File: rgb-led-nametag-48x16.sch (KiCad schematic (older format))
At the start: 41 parts, among them J1 USB_C_Receptacle_USB2.0, J2 TagConnect_TC2030_SWD, Q17 CJ3139K, Q18 CJ3139K, Q19 2SK3541, Q20 AO3401A, U25 STM32F722RETx, U26 SRV05-4, U27 TPS63001, U28 XC6206P332MR

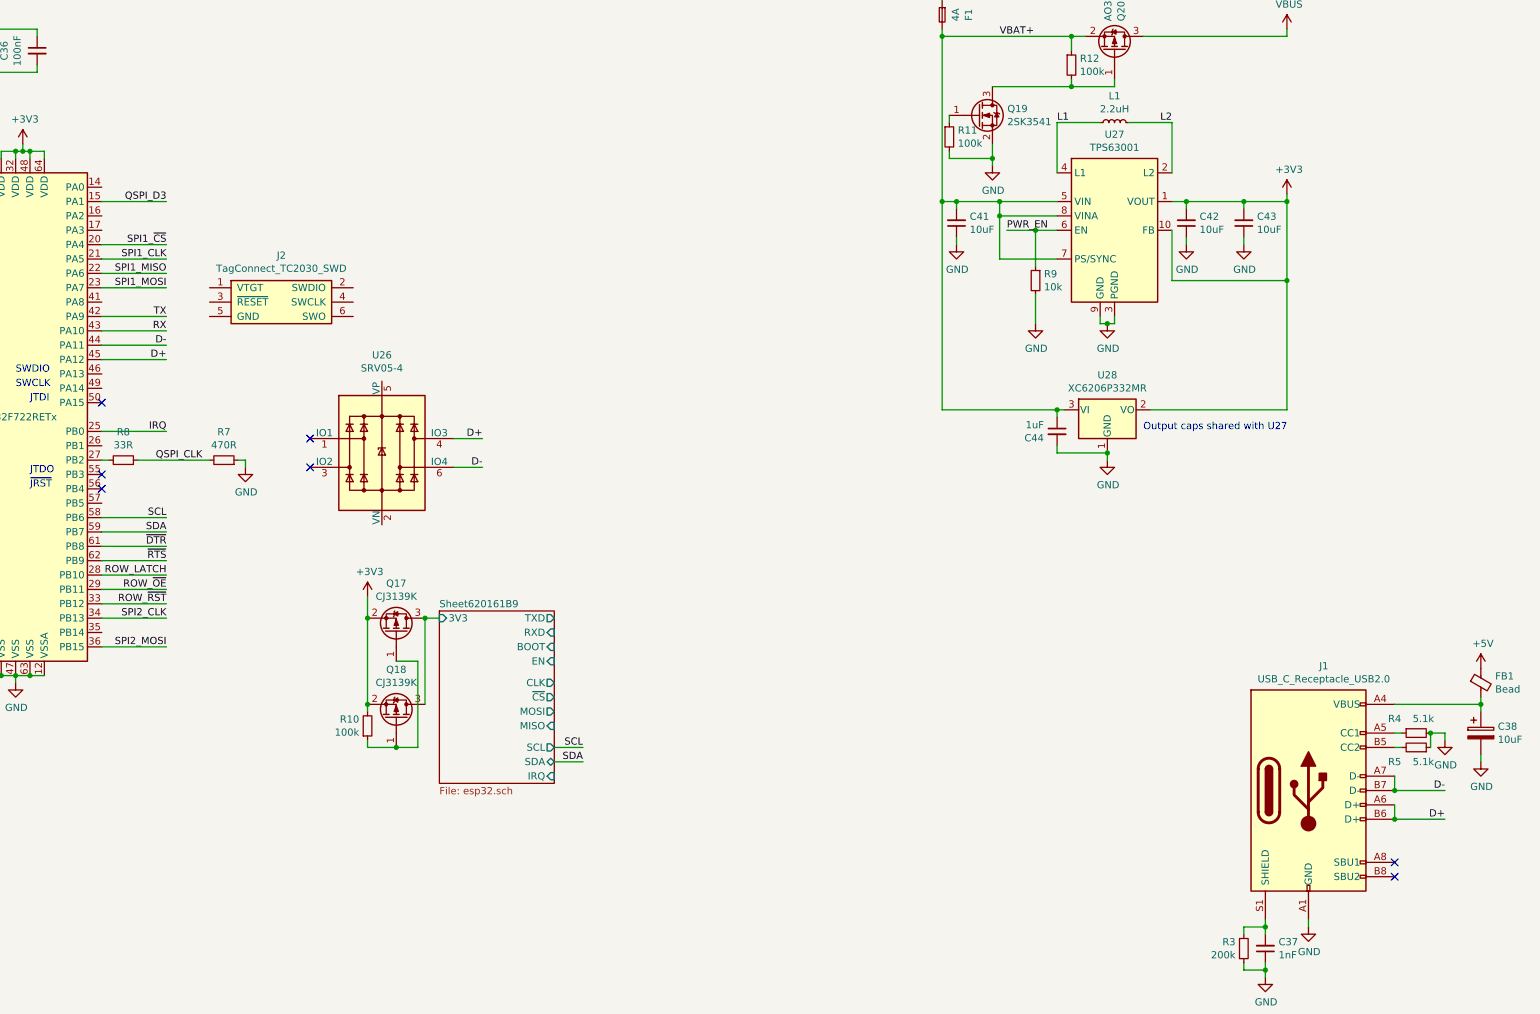
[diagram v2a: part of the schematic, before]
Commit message: Connect SWD to USB type C SBU
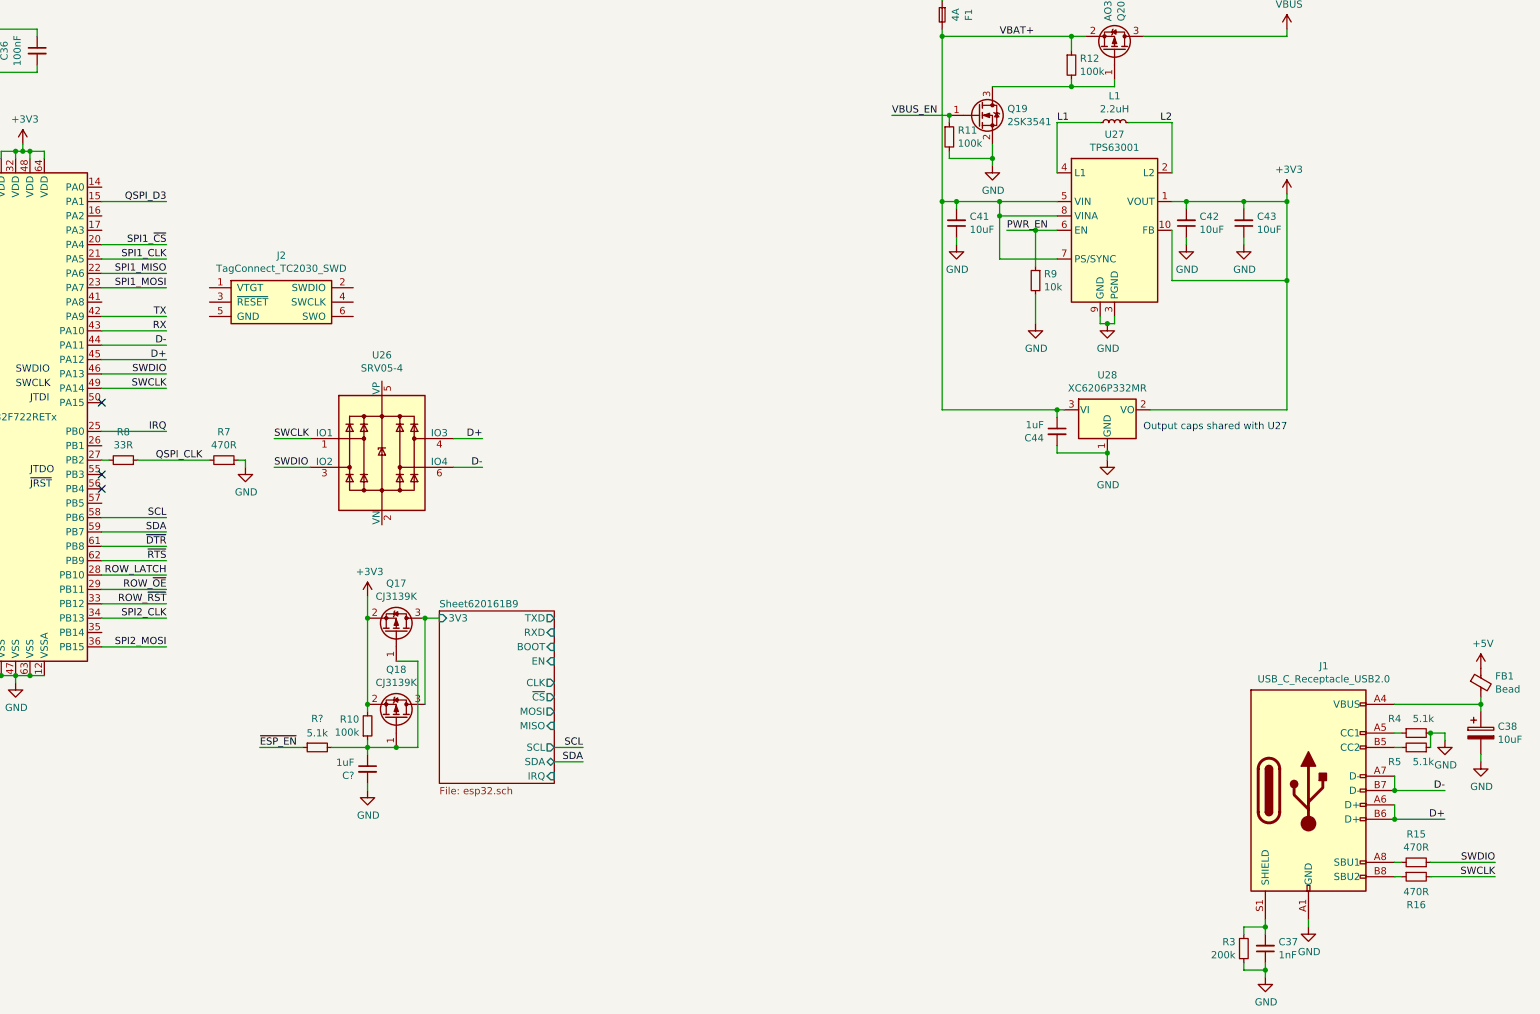
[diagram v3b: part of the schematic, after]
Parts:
- added C?: 1uF, Capacitor_SMD:C_0402_1005Metric, symbol Device:C_Small
- added R15, R16: 470R, Resistor_SMD:R_0402_1005Metric, symbol Device:R_Small
- added R?: 5.1k, Resistor_SMD:R_0402_1005Metric, symbol Device:R_Small
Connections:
- net GND: now also C?.2
- net SWDIO: now reaches U25.46 (PA13)
- net SWDIO: now also U26.3 (IO2), R15.1
- net SWCLK: now reaches U25.49 (PA14)
- net SWCLK: now also U26.1 (IO1), R16.2
- net at J1.A8 (SBU1): now also R15.2
- net at J1.B8 (SBU2): now also R16.1
- net at Q17.1 (G), Q18.1 (G), R10.1: now also C?.1, R?.2
- net VBUS_EN: now reaches Q19.1 (G), R11.1
- new net ~ESP_EN: R?.1
- no-connect marks 11 -> 7
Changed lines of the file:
@@
 D+
 Connection ~ 16400 6450
-NoConn ~ 16400 6750
-NoConn ~ 16400 6850
 $Comp
 L power:GND #PWR0176
@@
 	1    0    0    -1
 $EndComp
-NoConn ~ 8850 3800
-NoConn ~ 8850 4000
 $Comp
 L Device:R_Small R8
@@
 Wire Wire Line
 	10750 6050 10550 6050
-Wire Bus Line
-	2950 1250 2950 6650
 Wire Wire Line
 	14700 3600 15650 3600
 Text Notes 14650 3750 0    50   ~ 0
 Output caps shared with U27
+Wire Wire Line
+	7400 3350 7850 3350
+Text Label 7850 3350 2    50   ~ 0
+SWDIO
+Wire Wire Line
+	7400 3450 7850 3450
+Text Label 7850 3450 2    50   ~ 0
+SWCLK
+Wire Wire Line
+	16650 6750 17100 6750
+Text Label 17100 6750 2    50   ~ 0
+SWDIO
+Wire Wire Line
+	16650 6850 17100 6850
+Text Label 17100 6850 2    50   ~ 0
+SWCLK
+Text Label 8600 3800 0    50   ~ 0
+SWCLK
+Wire Wire Line
+	8600 3800 8850 3800
+$Comp
+L Device:R_Small R15
+U 1 1 62A6EAFE
+P 16550 6750
+F 0 "R15" V 16746 6750 50  0000 C CNN
+F 1 "470R" V 16655 6750 50  0000 C CNN
+F 2 "Resistor_SMD:R_0402_1005Metric" H 16550 6750 50  0001 C CNN
+F 3 "~" H 16550 6750 50  0001 C CNN
+F 4 "C25117" H 16550 6750 50  0001 C CNN "LCSC"
+	1    16550 6750
+	0    1    -1   0
+$EndComp
+$Comp
+L Device:R_Small R16
+U 1 1 62A82547
+P 16550 6850
+F 0 "R16" V 16746 6850 50  0000 C CNN
+F 1 "470R" V 16655 6850 50  0000 C CNN
+F 2 "Resistor_SMD:R_0402_1005Metric" H 16550 6850 50  0001 C CNN
+F 3 "~" H 16550 6850 50  0001 C CNN
+F 4 "C25117" H 16550 6850 50  0001 C CNN "LCSC"
+	1    16550 6850
+	0    -1   1    0
+$EndComp
+Wire Wire Line
+	16450 6750 16400 6750
+Wire Wire Line
+	16400 6850 16450 6850
+Wire Wire Line
+	8600 4000 8850 4000
+Text Label 8600 4000 0    50   ~ 0
+SWDIO
+$Comp
+L Device:C_Small C?
+U 1 1 62B47E57
+P 9250 6100
+AR Path="/620161BA/62B47E57" Ref="C?"  Part="1"
+AR Path="/62B47E57" Ref="C?"  Part="1"
+F 0 "C?" H 9158 6054 50  0000 R CNN
+F 1 "1uF" H 9158 6145 50  0000 R CNN
+F 2 "Capacitor_SMD:C_0402_1005Metric" H 9250 6100 50  0001 C CNN
+F 3 "~" H 9250 6100 50  0001 C CNN
+F 4 "C52923" H 9250 6100 50  0001 C CNN "LCSC"
+	1    9250 6100
+	1    0    0    -1
+$EndComp
+$Comp
+L power:GND #PWR?
+U 1 1 62B5C3F7
+P 9250 6250
+F 0 "#PWR?" H 9250 6000 50  0001 C CNN
+F 1 "GND" H 9255 6077 50  0000 C CNN
+F 2 "" H 9250 6250 50  0001 C CNN
+F 3 "" H 9250 6250 50  0001 C CNN
+	1    9250 6250
+	1    0    0    -1
+$EndComp
+Wire Wire Line
+	9250 6250 9250 6200
+Wire Wire Line
+	9250 6000 9250 5950
+Connection ~ 9250 5950
+$Comp
+L Device:R_Small R?
+U 1 1 62B8632F
+P 8900 5950
+F 0 "R?" V 8700 5950 50  0000 C CNN
+F 1 "5.1k" V 8800 5950 50  0000 C CNN
+F 2 "Resistor_SMD:R_0402_1005Metric" H 8900 5950 50  0001 C CNN
+F 3 "~" H 8900 5950 50  0001 C CNN
+F 4 "C23186" H 8900 5950 50  0001 C CNN "LCSC"
+	1    8900 5950
+	0    -1   1    0
+$EndComp
+Wire Wire Line
+	9000 5950 9250 5950
+Text Label 8500 5950 0    50   ~ 0
+~ESP_EN
+Wire Wire Line
+	8500 5950 8800 5950
+Connection ~ 13300 1550
+Text Label 12900 1550 0    50   ~ 0
+VBUS_EN
+Wire Wire Line
+	12900 1550 13300 1550
+Wire Bus Line
+	2950 1250 2950 6650
 $EndSCHEMATC

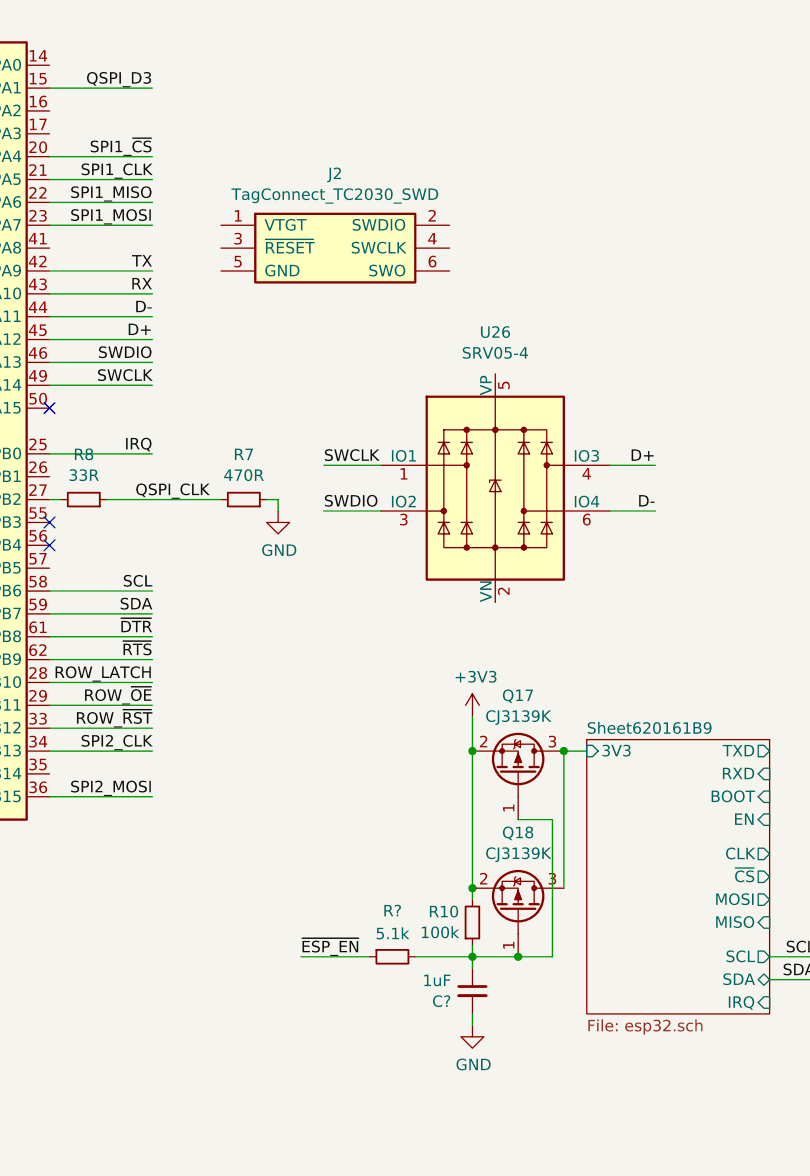
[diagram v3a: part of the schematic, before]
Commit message: Wire column mux SPI
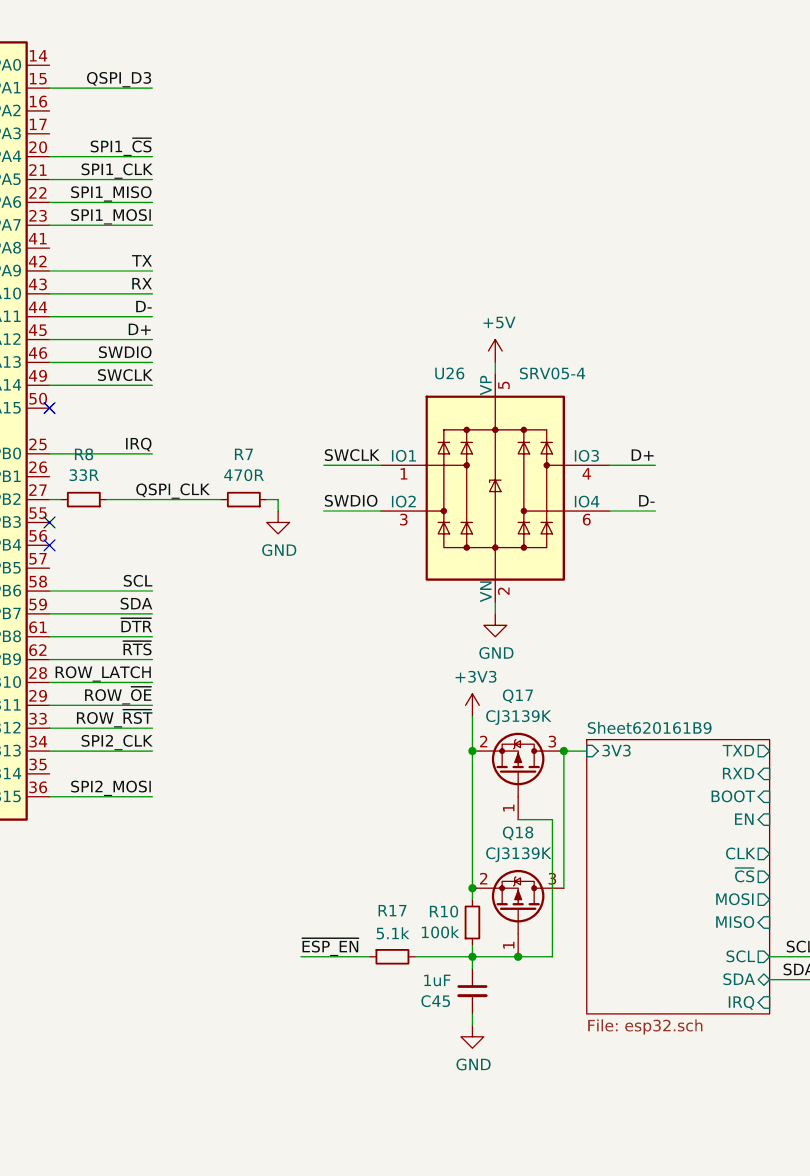
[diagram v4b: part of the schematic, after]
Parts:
- removed J2: TagConnect_TC2030_SWD, Connector:Tag-Connect_TC2030-IDC-NL_2x03_P1.27mm_Vertical, symbol Connector_TagConnect:TagConnect_TC2030_SWD
- gave numbers to parts that had none: 2
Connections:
- net +5V: now also U26.5 (VP)
- net GND: now also U26.2 (VN)
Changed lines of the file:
@@
 Text Label 7850 2750 2    50   ~ 0
 SPI1_MOSI
-Text Label 7850 5050 2    50   ~ 0
-SPI2_CLK
-Text Label 7850 5250 2    50   ~ 0
-SPI2_MOSI
 Text Label 1150 2900 0    50   ~ 0
 SPI2_MOSI
@@
 Wire Wire Line
 	6100 4450 5650 4450
-Text Label 7850 4750 2    50   ~ 0
-ROW_LATCH
-Wire Wire Line
-	7400 4750 7850 4750
 Text Label 7850 4850 2    50   ~ 0
 ROW_~OE
@@
 Wire Wire Line
 	7400 4650 7850 4650
-Wire Wire Line
-	7400 5050 7850 5050
-Wire Wire Line
-	7400 5250 7850 5250
 Wire Wire Line
 	7400 2750 7850 2750
@@
 Connection ~ 15500 7500
 $Comp
-L Connector_TagConnect:TagConnect_TC2030_SWD J2
-U 1 1 620AEB39
-P 8650 2850
-F 0 "J2" H 8650 3175 50  0000 C CNN
-F 1 "TagConnect_TC2030_SWD" H 8650 3084 50  0000 C CNN
-F 2 "Connector:Tag-Connect_TC2030-IDC-NL_2x03_P1.27mm_Vertical" H 8650 2850 50  0001 C CNN
-F 3 "" H 8650 2850 50  0001 C CNN
-	1    8650 2850
-	1    0    0    -1
-$EndComp
-$Comp
 L Regulator_Switching:TPS63001 U27
 U 1 1 620B2056
@@
 U 1 1 61FD5228
 P 9350 3900
-F 0 "U26" H 9350 4581 50  0000 C CNN
-F 1 "SRV05-4" H 9350 4490 50  0000 C CNN
+F 0 "U26" H 9150 4400 50  0000 C CNN
+F 1 "SRV05-4" H 9600 4400 50  0000 C CNN
 F 2 "Package_TO_SOT_SMD:SOT-23-6" H 10050 3450 50  0001 C CNN
 F 3 "http://www.onsemi.com/pub/Collateral/SRV05-4-D.PDF" H 9350 3900 50  0001 C CNN
@@
 P 9250 6100
 AR Path="/620161BA/62B47E57" Ref="C?"  Part="1"
-AR Path="/62B47E57" Ref="C?"  Part="1"
-F 0 "C?" H 9158 6054 50  0000 R CNN
+AR Path="/62B47E57" Ref="C45"  Part="1"
+F 0 "C45" H 9158 6054 50  0000 R CNN
 F 1 "1uF" H 9158 6145 50  0000 R CNN
 F 2 "Capacitor_SMD:C_0402_1005Metric" H 9250 6100 50  0001 C CNN
@@
 $EndComp
 $Comp
-L power:GND #PWR?
+L power:GND #PWR0198
 U 1 1 62B5C3F7
 P 9250 6250
-F 0 "#PWR?" H 9250 6000 50  0001 C CNN
+F 0 "#PWR0198" H 9250 6000 50  0001 C CNN
 F 1 "GND" H 9255 6077 50  0000 C CNN
 F 2 "" H 9250 6250 50  0001 C CNN
@@
 Connection ~ 9250 5950
 $Comp
-L Device:R_Small R?
+L Device:R_Small R17
 U 1 1 62B8632F
 P 8900 5950
-F 0 "R?" V 8700 5950 50  0000 C CNN
+F 0 "R17" V 8700 5950 50  0000 C CNN
 F 1 "5.1k" V 8800 5950 50  0000 C CNN
 F 2 "Resistor_SMD:R_0402_1005Metric" H 8900 5950 50  0001 C CNN
@@
 Wire Wire Line
 	12900 1550 13300 1550
+$Comp
+L power:+5V #PWR0199
+U 1 1 62C054E2
+P 9350 3350
+F 0 "#PWR0199" H 9350 3200 50  0001 C CNN
+F 1 "+5V" H 9365 3523 50  0000 C CNN
+F 2 "" H 9350 3350 50  0001 C CNN
+F 3 "" H 9350 3350 50  0001 C CNN
+	1    9350 3350
+	1    0    0    -1
+$EndComp
+Wire Wire Line
+	9350 3400 9350 3350
+$Comp
+L power:GND #PWR0200
+U 1 1 62C1B8E9
+P 9350 4450
+F 0 "#PWR0200" H 9350 4200 50  0001 C CNN
+F 1 "GND" H 9355 4277 50  0000 C CNN
+F 2 "" H 9350 4450 50  0001 C CNN
+F 3 "" H 9350 4450 50  0001 C CNN
+	1    9350 4450
+	1    0    0    -1
+$EndComp
+Wire Wire Line
+	7400 5050 7850 5050
+Text Label 7850 5050 2    50   ~ 0
+SPI2_CLK
+Wire Wire Line
+	7400 4750 7850 4750
+Text Label 7850 4750 2    50   ~ 0
+ROW_LATCH
+Wire Wire Line
+	9350 4450 9350 4400
 Wire Bus Line
 	2950 1250 2950 6650
+Text Label 7850 5250 2    50   ~ 0
+SPI2_MOSI
+Wire Wire Line
+	7400 5250 7850 5250
 $EndSCHEMATC
